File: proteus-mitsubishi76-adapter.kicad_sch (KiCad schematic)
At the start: 5 parts, among them J1 TE-3-178780-6

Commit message: Upd sch
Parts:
- removed J1: TE-3-178780-6, libs:TE-3-178780-6, symbol TE-3-178780-6_76P:TE-3-178780-6
- added BRD?: proteus, kicad6-libraries:proteus, symbol proteus:proteus
- added D? (x6): D_Schottky, Diode_SMD:D_SMA, symbol Device:D_Schottky
- added D?: DNP, Diode_SMD:D_SMA, symbol Device:D_Schottky
- added F? (x3): Fuse-Pad-Pad, hellen-one-common:PAD-1206-PAD, symbol hellen-one-common:Fuse-Pad-Pad
- added G? (x7): PROTO_AREA, hellen-one-common:PROTO_AREA, symbol hellen-one-common:PROTO_AREA
- added G?: RUSEFI_LOGO, kicad6-libraries:rusefi_logo, symbol rusefi_logo:RUSEFI_LOGO
- added J?: TE-3-178780-6, kicad6-libraries:TE-3-178780-6, symbol TE-3-178780-6:TE-3-178780-6
- added J?: Conn_01x01, TestPoint:TestPoint_Pad_D4.0mm, symbol Connector_Generic:Conn_01x01
- added P? (x33): Pad, hellen-one-common:PAD-TH, symbol hellen-one-common:Pad
- added Q? (x4): AUIPS2041LTR, Package_TO_SOT_SMD:SOT-223, symbol Power_Management:AUIPS2041L
- added R? (x4): 10k, Resistor_SMD:R_0402_1005Metric, symbol Device:R
- added R? (x5): Jumper-Pad-Pad, hellen-one-common:PAD-0805-PAD, symbol hellen-one-common:Jumper-Pad-Pad
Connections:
- new net: J?.56, P?.1 (Pin_1)
- new net: G?.1, G?.11, G?.6 (x6)
- new net: G?.10, G?.15, G?.5 (x6)
- new net: G?.12, G?.2, G?.7 (x6)
- new net: G?.13, G?.3, G?.8 (x6)
- new net: G?.14, G?.4, G?.9 (x6)
- new net: F?.1, J?.25
- new net: J?.33, P?.1 (Pin_1)
- new net: J?.52, P?.1 (Pin_1)
- new net: J?.39, R?.1
- new net: J?.80, P?.1 (Pin_1)
- new net: J?.57, P?.1 (Pin_1)
- new net: J?.55, P?.1 (Pin_1)
- new net: J?.46, P?.1 (Pin_1)
- new net: J?.44, P?.1 (Pin_1)
- new net: J?.42, P?.1 (Pin_1)
- new net: J?.34, P?.1 (Pin_1)
- new net: J?.9, P?.1 (Pin_1)
- new net: J?.53, P?.1 (Pin_1)
- new net: J?.79, P?.1 (Pin_1)
- new net: J?.91, R?.1
- new net: J?.6, P?.1 (Pin_1)
- new net: J?.11, R?.1, R?.1
- new net: F?.1, J?.12
- new net: J?.24, P?.1 (Pin_1)
- new net: J?.31, R?.1
- new net: J?.35, P?.1 (Pin_1)
- new net: J?.37, P?.1 (Pin_1)
- new net: J?.41, P?.1 (Pin_1)
- new net: J?.43, P?.1 (Pin_1)
- new net: J?.45, P?.1 (Pin_1)
- new net: J?.51, P?.1 (Pin_1)
- new net: J?.54, P?.1 (Pin_1)
- new net: J?.58, P?.1 (Pin_1)
- new net: J?.59, P?.1 (Pin_1)
- new net: J?.60, P?.1 (Pin_1)
- new net: J?.61, P?.1 (Pin_1)
- new net: J?.62, P?.1 (Pin_1)
- new net: J?.7, P?.1 (Pin_1)
- new net: J?.74, P?.1 (Pin_1)
- new net: J?.75, P?.1 (Pin_1)
- new net: J?.76, P?.1 (Pin_1)
- new net: J?.77, P?.1 (Pin_1)
- new net: F?.1, J?.82
- new net: J?.87, P?.1 (Pin_1)
- new net +5VA: BRD?.C21(15) (5V_1), BRD?.C32(27) (5V_1), BRD?.C9(4) (5V_1), G?.10, G?.6, G?.7, G?.8, G?.9, J?.81
- new net 12V_IGN: BRD?.B18(21) (12V_IGN), F?.2
- new net 12V_MR: BRD?.B23(16) (12V_MR), D?.1 (K), D?.1 (K), D?.1 (K), D?.1 (K), D?.1 (K), D?.1 (K), D?.1 (K), F?.2, F?.2
- new net 12V_PROT: BRD?.C11(2) (12V_PROT), BRD?.C12(1) (12V_PROT), G?.11, G?.12, G?.13, G?.14, G?.15
- new net GND: BRD?.A17(19) (GND), BRD?.A18(18) (GND), BRD?.A24(35) (GND), BRD?.B14(10) (GND), BRD?.B19(20) (GND), BRD?.B20(19) (GND), BRD?.C1(12) (GND_SENS), BRD?.C2(11) (GND_SENS), BRD?.C23(13) (GND_SENS), BRD?.C29(30) (GND_SENS), BRD?.C3(10) (GND_SENS), BRD?.C4(9) (GND_SENS), BRD?.C5(8) (GND_SENS), BRD?.C6(7) (GND_SENS), BRD?.C7(6) (GND_SENS), BRD?.C8(5) (GND_SENS), G?.1, G?.2, G?.3, G?.4, G?.5, J?.1 (Pin_1), J?.13, J?.26, J?.40, J?.92, Q?.3 (S), Q?.3 (S), Q?.3 (S), Q?.3 (S), R?.1, R?.1, R?.1, R?.1, R?.2
- new net IDLE1: BRD?.A28(31) (IGN9), Q?.1 (IN), R?.2
- new net IDLE2: BRD?.A27(32) (IGN10), Q?.1 (IN), R?.2
- new net IDLE3: BRD?.A26(33) (IGN11), Q?.1 (IN), R?.2
- new net IDLE4: BRD?.A25(34) (IGN12), Q?.1 (IN), R?.2
- new net IN_CAM: BRD?.B2(7) (D3), J?.88
- new net IN_CLT: BRD?.C20(16) (AT3(CLT)), J?.83
- new net IN_CRANK: BRD?.B3(6) (D4), J?.89
- new net IN_EGR_TEMP/MANIFOLD_FIFF_PRESSURE: BRD?.C19(17) (AT1), J?.73
- new net IN_IAT: BRD?.C30(29) (AT2(IAT)), J?.72
- new net IN_KNOCK: BRD?.C34(25) (KNOCK1), J?.78
- new net IN_MAF: BRD?.C14(22) (AV3), J?.90
- new net IN_MAP: BRD?.C13(23) (AV1(MAP)), J?.85
- new net IN_STARTER_RELAY: BRD?.B10(14) (D1), J?.71
- new net IN_TPS: BRD?.C24(35) (AV2(TPS)), J?.84
- new net IN_VAF: BRD?.C25(34) (AV4), J?.19
- new net IN_VSS: BRD?.B1(8) (D2), J?.86
- new net MAGNETIC_CLUTCH_RELAY/FUEL_PUMP_RELAY: BRD?.A7(6) (LS7(INJ7)), J?.22
- new net OUT_CHECK_ENGINE: BRD?.A9(4) (LS11(INJ11)), J?.36
- new net OUT_FAN_RELAY_HI: BRD?.A11(2) (LS14), J?.20
- new net OUT_FAN_RELAY_LOW/AC: BRD?.A12(1) (LS15(FAN)), J?.21
- new net OUT_FUEL_PUMP_HI/LO_RELAY: BRD?.A19(17) (LS8(INJ8)), R?.2, R?.2
- new net OUT_FUEL_PUMP_RELAY/AC: BRD?.A23(13) (LS16(FUEL)), J?.8
- new net OUT_IDLE1: D?.2 (A), J?.4, Q?.2 (D)
- new net OUT_IDLE2: D?.2 (A), J?.5, Q?.2 (D)
- new net OUT_IDLE3: D?.2 (A), J?.17, Q?.2 (D)
- new net OUT_IDLE4: D?.2 (A), J?.18, Q?.2 (D)
- new net OUT_IGN1: BRD?.A35(24) (IGN1), J?.10
- new net OUT_IGN2: BRD?.A34(25) (IGN2), J?.23
- new net OUT_IGN3: BRD?.A22(14) (IGN3), R?.2
- new net OUT_INJ1: BRD?.A3(10) (LS1(INJ1)), J?.1
- new net OUT_INJ2: BRD?.A15(21) (LS2(INJ2)), J?.14
- new net OUT_INJ3: BRD?.A4(9) (LS3(INJ3)), J?.2
- new net OUT_INJ4: BRD?.A16(20) (LS4(INJ4)), J?.15
- new net OUT_INJ5/FUEL_PRESS_SOLENOID: BRD?.A5(8) (LS5(INJ5)), J?.3
- new net OUT_INJ6/TURBOCHRG_WG_SOLEOID: BRD?.A6(7) (LS6(INJ6)), D?.2 (A), J?.16
- new net OUT_MAIN_RELAY: BRD?.A10(3) (LS13(MAIN)), J?.38
- new net OUT_TURBOCHRG_WG_SOLENOID/AC: BRD?.A20(16) (LS10(INJ10)), D?.2 (A), J?.32
- new net OUT_WG_SOLENOID: BRD?.A8(5) (LS9(INJ9)), D?.2 (A), R?.2
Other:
- note added: "12V Bat"
- note added: "???"
- note added: "AC???"
- note added: "Connectors 776228-1 776231-1 776231-2 Mating plugs 770680-1 776164-1 776164-2 Terminals 770854-1 all of the above cheap from ttiinc.com"
- note added: "FUEL TEMP"
- moved on the sheet: H1, H2, H3, H4

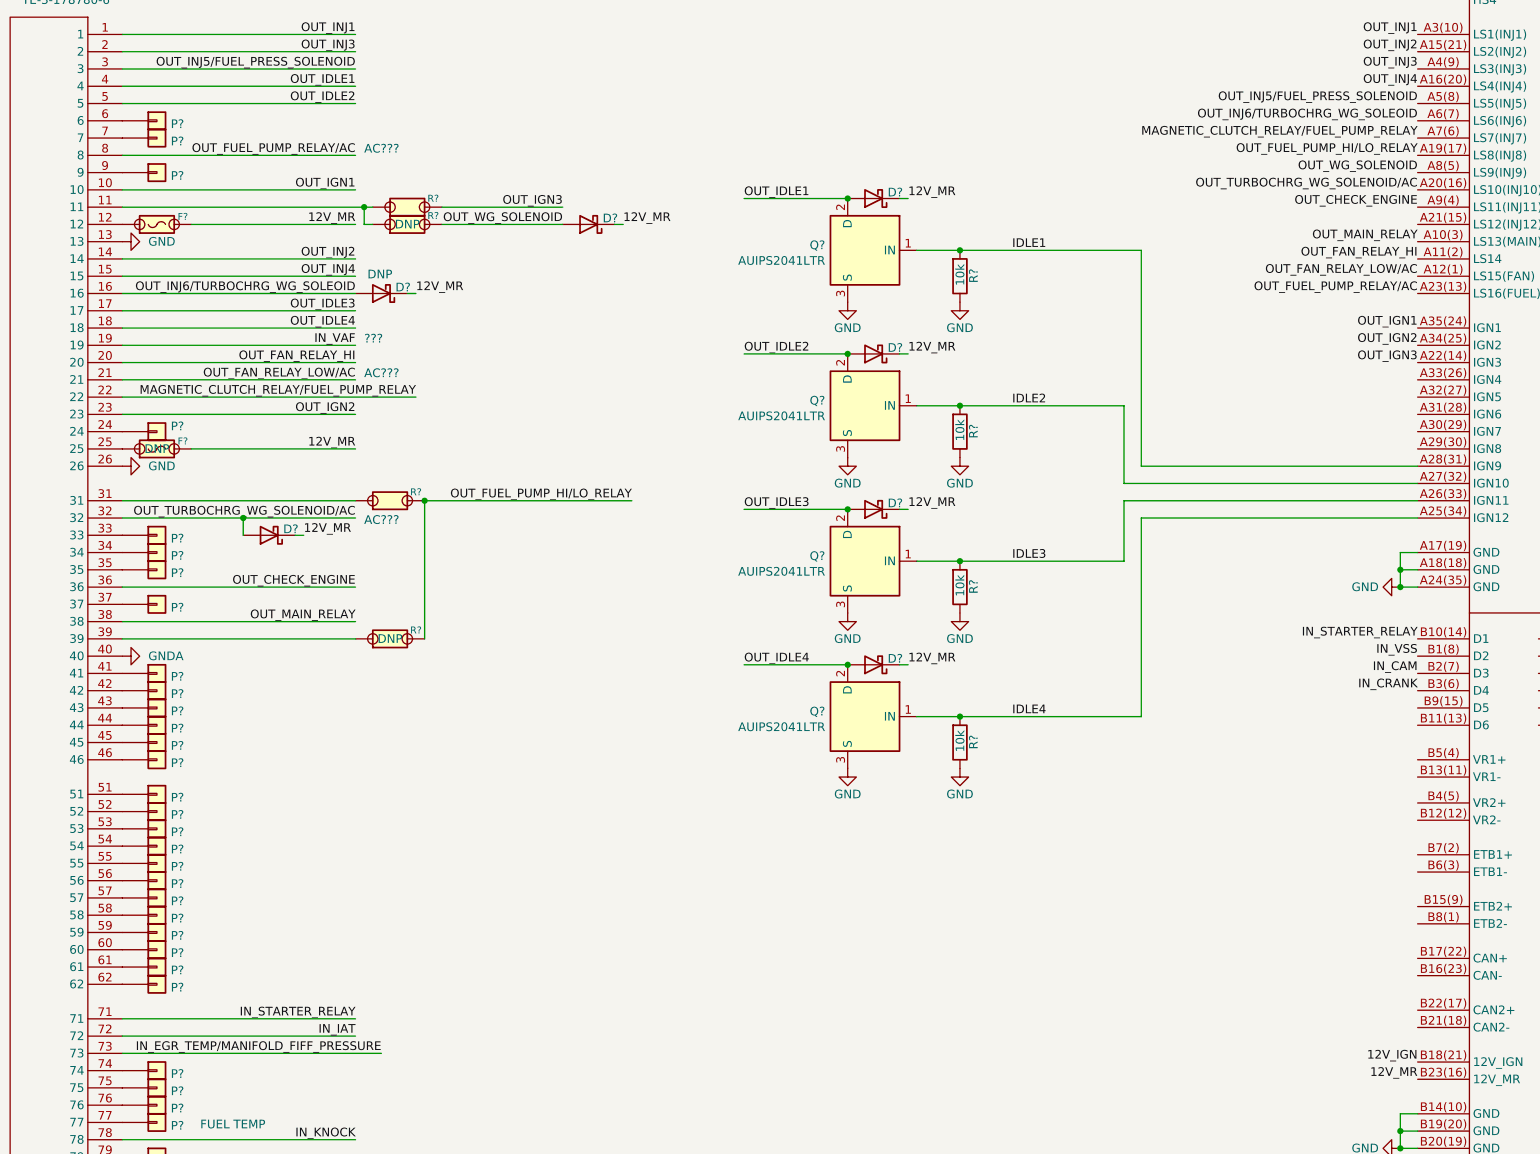
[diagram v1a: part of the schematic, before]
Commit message: Starter pin, 8/22 pins note
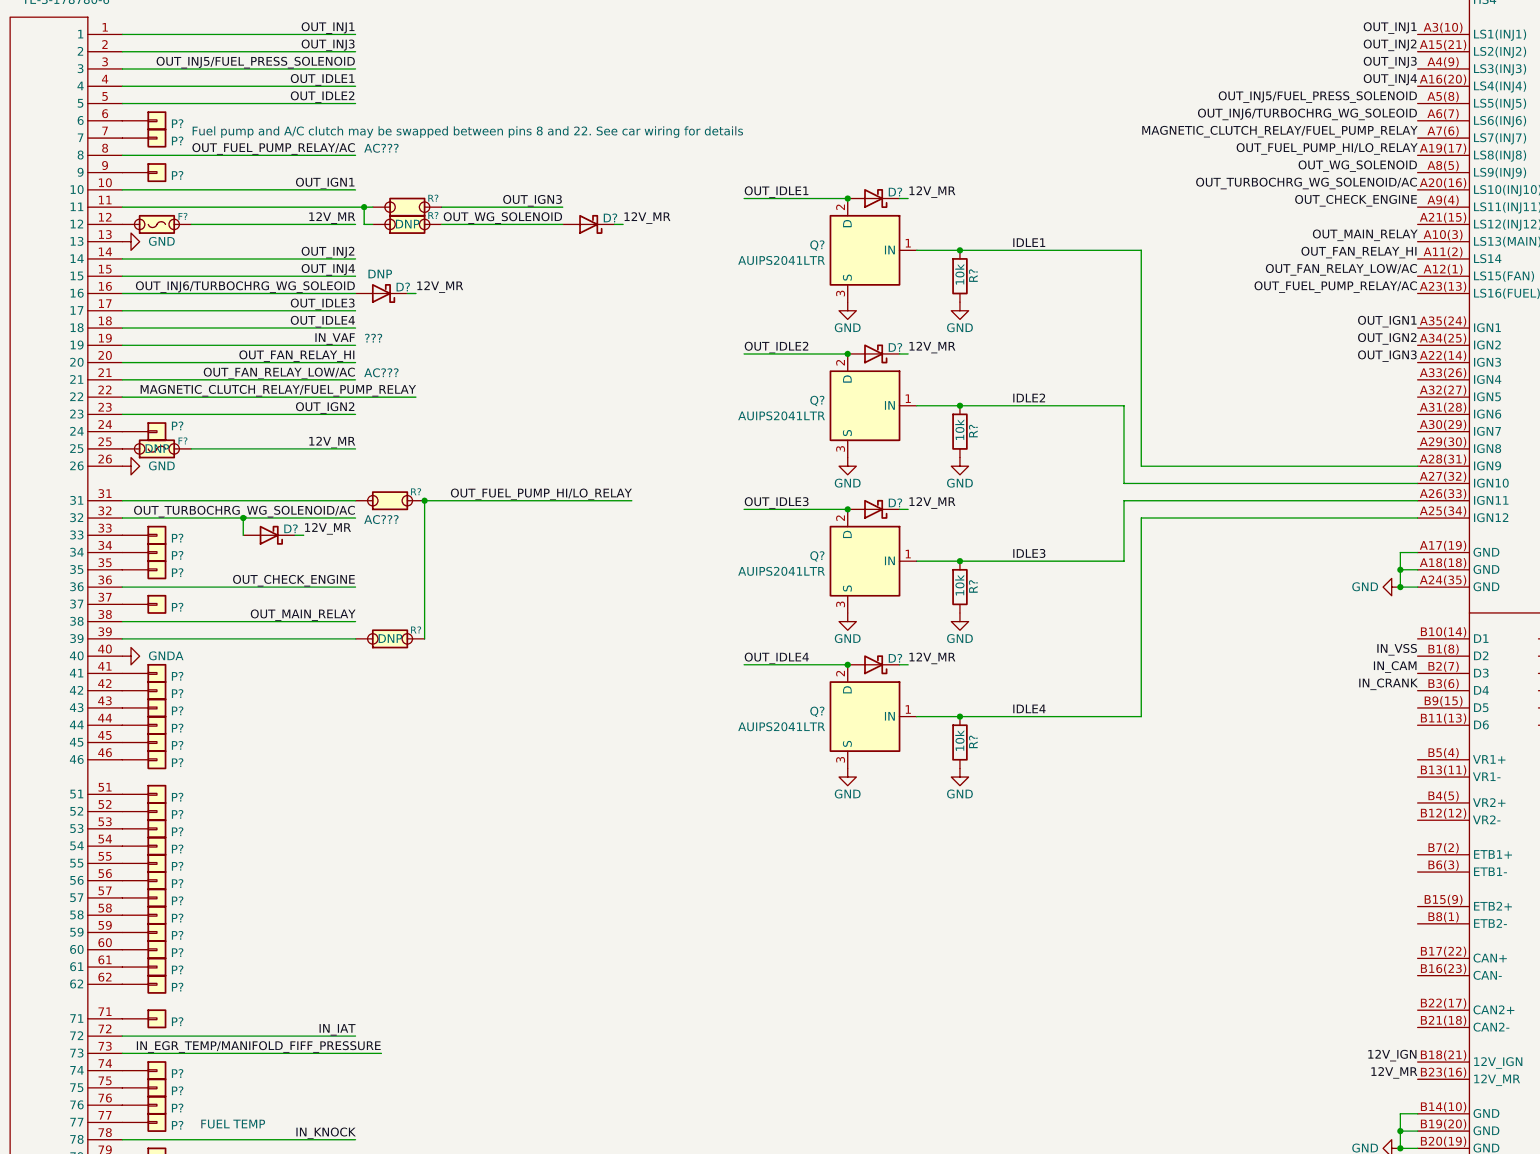
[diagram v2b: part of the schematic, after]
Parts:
- added P?: Pad, hellen-one-common:PAD-TH, symbol hellen-one-common:Pad
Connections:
- net IN_STARTER_RELAY: no longer names the net of BRD?.B10(14) (D1)
- net IN_STARTER_RELAY: no longer J?.71
- new net: J?.71, P?.1 (Pin_1)
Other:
- note added: "Fuel pump and A/C clutch may be swapped between pins 8 and 22. See car wiring for details"

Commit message: Upd sch
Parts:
- added J1: XH-10AW, Connector_JST:JST_XH_S10B-XH-A_1x10_P2.50mm_Horizontal, symbol Connector_Generic:Conn_01x10
- added J3: XH-10A, Connector_JST:JST_XH_B10B-XH-A_1x10_P2.50mm_Vertical, symbol Connector_Generic:Conn_01x10
- added J4: Conn_01x06, Connector_PinHeader_2.54mm:PinHeader_1x06_P2.54mm_Vertical, symbol Connector_Generic:Conn_01x06
- added M1: Module-wbo-0.3, hellen-one-wbo-0.3:wbo, symbol hellen-one-wbo-0.3:Module-wbo-0.3
- added M2: Module-can-0.1, hellen-one-can-0.1:can, symbol hellen-one-can-0.1:Module-can-0.1
- added P35, P36, P37, P38, P39, P40, P41, P42, P43, P44, P45, P46, P47, P48, P49, P50, P51, P52, P53, P54, P55, P56, P57, P58, P59, P60, P61, P62, P63, P64, P65, P66, P67: Pad, hellen-one-common:PAD-TH, symbol hellen-one-common:Pad
- added R1, R10, R11, R12, R13, R14, R15, R16, R17, R18, R19, R2, R20, R21, R22, R23, R24, R25, R26, R27, R28, R29, R3, R30, R32, R4, R5, R6, R7, R8, R9: Jumper-Pad-Pad, hellen-one-common:PAD-0805-PAD, symbol hellen-one-common:Jumper-Pad-Pad
- gave numbers to parts that had none: 68
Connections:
- net +5VA: now also M1.W1 (V5_IN), M2.V1 (V5)
- net 12V_MR: now also J1.1 (Pin_1), J1.2 (Pin_2), J3.1 (Pin_1), J3.2 (Pin_2)
- net GND: now also J1.10 (Pin_10), J1.9 (Pin_9), J3.10 (Pin_10), J3.9 (Pin_9), J4.3 (Pin_3), M1.E6 (LSU_H-), M1.G (GND), M2.E1 (GND)
- net IN_CAM: now also R28.2; no longer J2.88
- net IN_CLT: now also R25.2; no longer J2.83
- net IN_CRANK: now also R29.2; no longer J2.89
- net IN_EGR_TEMP/MANIFOLD_FIFF_PRESSURE: now also R23.2; no longer J2.73
- net IN_IAT: now also R22.2; no longer J2.72
- net IN_KNOCK: now also R24.2; no longer J2.78
- net IN_MAF: now also R30.2; no longer J2.90
- net IN_MAP: now also R26.2; no longer J2.85
- net IN_TPS: now also R32.2; no longer J2.84
- net IN_VAF: now also R14.2; no longer J2.19
- net IN_VSS: now also R27.2; no longer J2.86
- net MAGNETIC_CLUTCH_RELAY/FUEL_PUMP_RELAY: now also R17.2; no longer J2.22
- net OUT_CHECK_ENGINE: now also R20.2; no longer J2.36
- net OUT_FAN_RELAY_HI: now also R15.2; no longer J2.20
- net OUT_FAN_RELAY_LOW/AC: now also R16.2; no longer J2.21
- net OUT_FUEL_PUMP_RELAY/AC: now also R6.2; no longer J2.8
- net OUT_IDLE1: now also R4.2; no longer J2.4
- net OUT_IDLE2: now also R5.2; no longer J2.5
- net OUT_IDLE3: now also R12.2; no longer J2.17
- net OUT_IDLE4: now also R13.2; no longer J2.18
- net OUT_IGN1: now also R7.2; no longer J2.10
- net OUT_IGN2: now also R18.2; no longer J2.23
- net OUT_INJ1: now also R1.2; no longer J2.1
- net OUT_INJ2: now also R9.2; no longer J2.14
- net OUT_INJ3: now also R2.2; no longer J2.2
- net OUT_INJ4: now also R10.2; no longer J2.15
- net OUT_INJ5/FUEL_PRESS_SOLENOID: now also R3.2; no longer J2.3
- net OUT_INJ6/TURBOCHRG_WG_SOLEOID: now also R11.2; no longer J2.16
- net OUT_MAIN_RELAY: now also R21.2; no longer J2.38
- net OUT_TURBOCHRG_WG_SOLENOID/AC: now also R19.2; no longer J2.32
- net at BRD1.A1(12) (HS2): now also P41.1 (Pin_1)
- net at BRD1.A13(23) (HS3): now also P42.1 (Pin_1)
- net at BRD1.A14(22) (HS4): now also P43.1 (Pin_1)
- net at BRD1.A2(11) (HS1): now also P40.1 (Pin_1)
- net at BRD1.A21(15) (LS12(INJ12)): now also P35.1 (Pin_1)
- net at BRD1.A29(30) (IGN8): now also P48.1 (Pin_1)
- net at BRD1.A30(29) (IGN7): now also P47.1 (Pin_1)
- net at BRD1.A31(28) (IGN6): now also P46.1 (Pin_1)
- net at BRD1.A32(27) (IGN5): now also P45.1 (Pin_1)
- net at BRD1.A33(26) (IGN4): now also P44.1 (Pin_1)
- net at BRD1.B10(14) (D1): now also P36.1 (Pin_1)
- net at BRD1.B11(13) (D6): now also P38.1 (Pin_1)
- net at BRD1.B12(12) (VR2-): now also P52.1 (Pin_1)
- net at BRD1.B13(11) (VR1-): now also P50.1 (Pin_1)
- net at BRD1.B15(9) (ETB2+): now also P55.1 (Pin_1)
- net CAN_L: now reaches BRD1.B16(23) (CAN-)
- net CAN_L: now also M2.S1 (CANL)
- net CAN_H: now reaches BRD1.B17(22) (CAN+)
- net CAN_H: now also M2.S2 (CANH)
- net at BRD1.B21(18) (CAN2-): now also P58.1 (Pin_1)
- net at BRD1.B22(17) (CAN2+): now also P57.1 (Pin_1)
- net at BRD1.B4(5) (VR2+): now also P51.1 (Pin_1)
- net at BRD1.B5(4) (VR1+): now also P49.1 (Pin_1)
- net at BRD1.B6(3) (ETB1-): now also P54.1 (Pin_1)
- net at BRD1.B7(2) (ETB1+): now also P53.1 (Pin_1)
- net at BRD1.B8(1) (ETB2-): now also P56.1 (Pin_1)
- net at BRD1.B9(15) (D5): now also P37.1 (Pin_1)
- net at BRD1.C10(3) (5V_2): now also BRD1.C22(14) (5V_2), BRD1.C33(26) (5V_2), P39.1 (Pin_1)
- net at BRD1.C15(21) (AV5): now also P59.1 (Pin_1)
- net at BRD1.C16(20) (AV7): now also P61.1 (Pin_1)
- net at BRD1.C17(19) (AV9): now also P63.1 (Pin_1)
- net at BRD1.C18(18) (AV11): now also P65.1 (Pin_1)
- net at BRD1.C26(33) (AV6): now also P60.1 (Pin_1)
- net at BRD1.C27(32) (AV8): now also P62.1 (Pin_1)
- net at BRD1.C28(31) (AV10): now also P64.1 (Pin_1)
- net at BRD1.C31(28) (AT4): now also P66.1 (Pin_1)
- net at BRD1.C35(24) (KNOCK2): now also P67.1 (Pin_1)
- net at R33.1, R34.1: now also R8.2; no longer J2.11
- new net: J2.90, R30.1
- new net: J2.16, R11.1
- new net: J2.2, R2.1
- new net: J2.36, R20.1
- new net: J2.73, R23.1
- new net: J2.20, R15.1
- new net: J2.22, R17.1
- new net: J2.19, R14.1
- new net: J2.83, R25.1
- new net: J2.10, R7.1
- new net: J2.18, R13.1
- new net: J2.78, R24.1
- new net: J2.85, R26.1
- new net: J2.21, R16.1
- new net: J2.72, R22.1
- new net: J2.89, R29.1
- new net: J2.8, R6.1
- new net: J2.1, R1.1
- new net: J2.11, R8.1
- new net: J2.14, R9.1
- new net: J2.15, R10.1
- new net: J2.17, R12.1
- new net: J2.23, R18.1
- new net: J2.3, R3.1
- new net: J2.32, R19.1
- new net: J2.38, R21.1
- new net: J2.4, R4.1
- new net: J2.5, R5.1
- new net: J2.84, R32.1
- new net: J2.86, R27.1
- new net: J2.88, R28.1
- new net: M1.J1 (SEL1), M1.J_GND1 (PULL_DOWN1)
- new net: M1.W2 (CAN_VIO), M2.V2 (CAN_VIO)
- new net: M1.W3 (CAN_RX), M2.V6 (CAN_RX)
- new net: M1.W4 (CAN_TX), M2.V5 (CAN_TX)
- new net: J4.5 (Pin_5), M1.W5 (nReset)
- new net: J4.4 (Pin_4), M1.W6 (SWDIO)
- new net: J4.2 (Pin_2), M1.W7 (SWCLK)
- new net: J4.1 (Pin_1), M1.W8 (V33_OUT)
- new net WBO_H-: J1.7 (Pin_7), J1.8 (Pin_8), J3.7 (Pin_7), J3.8 (Pin_8), M1.E5 (LSU_H+)
- new net WBO_Ip: J1.5 (Pin_5), J3.5 (Pin_5), M1.E3 (LSU_Ip)
- new net WBO_R_Trim: J1.6 (Pin_6), J3.6 (Pin_6), M1.E4 (LSU_Rtrim)
- new net WBO_Vs: J1.3 (Pin_3), J3.3 (Pin_3), M1.E1 (LSU_Un)
- new net WBO_Vs/Ip: J1.4 (Pin_4), J3.4 (Pin_4), M1.E2 (LSU_Vm)
- no-connect marks 0 -> 5
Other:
- note added: "#0"
- moved on the sheet: D1, D2, R35, R36
